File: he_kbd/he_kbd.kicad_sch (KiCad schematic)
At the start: 270 parts, among them J1 AudioJack4, J2 Conn_01x08_Pin, J3 AudioJack4, J4 Conn_01x08_Pin

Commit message: updated backside / right hand board swithc footprints to have no holes
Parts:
- HE_36, HE_37, HE_38, HE_39, HE_40, HE_41, HE_42, HE_43, HE_44, HE_45, HE_46, HE_47, HE_48, HE_49, HE_50, HE_51, HE_52, HE_53, HE_54, HE_55, HE_56, HE_57, HE_58, HE_59, HE_60, HE_61, HE_62, HE_63, HE_64, HE_65, HE_66, HE_67, HE_68, HE_69, HE_70: footprint he_kbd_footprint:Analogue_sensor_and_switch_profile -> he_kbd_footprint:Analogue_sensor_and_switch_profile_NO_HOLES
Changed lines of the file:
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@@
 			)
 		)
-		(property "Footprint" "he_kbd_footprint:Analogue_sensor_and_switch_profile"
+		(property "Footprint" "he_kbd_footprint:Analogue_sensor_and_switch_profile_NO_HOLES"
 			(at 472.186 107.696 0)
 			(effects
@@
 			)
 		)
-		(property "Footprint" "he_kbd_footprint:Analogue_sensor_and_switch_profile"
+		(property "Footprint" "he_kbd_footprint:Analogue_sensor_and_switch_profile_NO_HOLES"
 			(at 472.186 126.746 0)
 			(effects
@@
 			)
 		)
-		(property "Footprint" "he_kbd_footprint:Analogue_sensor_and_switch_profile"
+		(property "Footprint" "he_kbd_footprint:Analogue_sensor_and_switch_profile_NO_HOLES"
 			(at 557.276 120.396 0)
 			(effects
@@
 			)
 		)
-		(property "Footprint" "he_kbd_footprint:Analogue_sensor_and_switch_profile"
+		(property "Footprint" "he_kbd_footprint:Analogue_sensor_and_switch_profile_NO_HOLES"
 			(at 557.276 107.696 0)
 			(effects
@@
 			)
 		)
-		(property "Footprint" "he_kbd_footprint:Analogue_sensor_and_switch_profile"
+		(property "Footprint" "he_kbd_footprint:Analogue_sensor_and_switch_profile_NO_HOLES"
 			(at 435.864 86.614 0)
 			(effects
@@
 			)
 		)
-		(property "Footprint" "he_kbd_footprint:Analogue_sensor_and_switch_profile"
+		(property "Footprint" "he_kbd_footprint:Analogue_sensor_and_switch_profile_NO_HOLES"
 			(at 520.954 118.364 0)
 			(effects
@@
 			)
 		)
-		(property "Footprint" "he_kbd_footprint:Analogue_sensor_and_switch_profile"
+		(property "Footprint" "he_kbd_footprint:Analogue_sensor_and_switch_profile_NO_HOLES"
 			(at 520.954 131.064 0)
 			(effects
@@
 			)
 		)
-		(property "Footprint" "he_kbd_footprint:Analogue_sensor_and_switch_profile"
+		(property "Footprint" "he_kbd_footprint:Analogue_sensor_and_switch_profile_NO_HOLES"
 			(at 435.864 112.014 0)
 			(effects
@@
 			)
 		)
-		(property "Footprint" "he_kbd_footprint:Analogue_sensor_and_switch_profile"
+		(property "Footprint" "he_kbd_footprint:Analogue_sensor_and_switch_profile_NO_HOLES"
 			(at 520.954 112.014 0)
 			(effects
@@
 			)
 		)
-		(property "Footprint" "he_kbd_footprint:Analogue_sensor_and_switch_profile"
+		(property "Footprint" "he_kbd_footprint:Analogue_sensor_and_switch_profile_NO_HOLES"
 			(at 520.954 105.664 0)
 			(effects
@@
 			)
 		)
-		(property "Footprint" "he_kbd_footprint:Analogue_sensor_and_switch_profile"
+		(property "Footprint" "he_kbd_footprint:Analogue_sensor_and_switch_profile_NO_HOLES"
 			(at 557.276 114.046 0)
 			(effects
@@
 			)
 		)
-		(property "Footprint" "he_kbd_footprint:Analogue_sensor_and_switch_profile"
+		(property "Footprint" "he_kbd_footprint:Analogue_sensor_and_switch_profile_NO_HOLES"
 			(at 634.746 107.696 0)
 			(effects
@@
 			)
 		)
-		(property "Footprint" "he_kbd_footprint:Analogue_sensor_and_switch_profile"
+		(property "Footprint" "he_kbd_footprint:Analogue_sensor_and_switch_profile_NO_HOLES"
 			(at 472.186 133.096 0)
 			(effects
@@
 			)
 		)
-		(property "Footprint" "he_kbd_footprint:Analogue_sensor_and_switch_profile"
+		(property "Footprint" "he_kbd_footprint:Analogue_sensor_and_switch_profile_NO_HOLES"
 			(at 435.864 92.964 0)
 			(effects
@@
 			)
 		)
-		(property "Footprint" "he_kbd_footprint:Analogue_sensor_and_switch_profile"
+		(property "Footprint" "he_kbd_footprint:Analogue_sensor_and_switch_profile_NO_HOLES"
 			(at 557.276 139.446 0)
 			(effects
@@
 			)
 		)
-		(property "Footprint" "he_kbd_footprint:Analogue_sensor_and_switch_profile"
+		(property "Footprint" "he_kbd_footprint:Analogue_sensor_and_switch_profile_NO_HOLES"
 			(at 634.746 101.346 0)
 			(effects
@@
 			)
 		)
-		(property "Footprint" "he_kbd_footprint:Analogue_sensor_and_switch_profile"
+		(property "Footprint" "he_kbd_footprint:Analogue_sensor_and_switch_profile_NO_HOLES"
 			(at 557.276 94.996 0)
 			(effects
@@
 			)
 		)
-		(property "Footprint" "he_kbd_footprint:Analogue_sensor_and_switch_profile"
+		(property "Footprint" "he_kbd_footprint:Analogue_sensor_and_switch_profile_NO_HOLES"
 			(at 520.954 124.714 0)
 			(effects
@@
 			)
 		)
-		(property "Footprint" "he_kbd_footprint:Analogue_sensor_and_switch_profile"
+		(property "Footprint" "he_kbd_footprint:Analogue_sensor_and_switch_profile_NO_HOLES"
 			(at 435.864 118.364 0)
 			(effects
@@
 			)
 		)
-		(property "Footprint" "he_kbd_footprint:Analogue_sensor_and_switch_profile"
+		(property "Footprint" "he_kbd_footprint:Analogue_sensor_and_switch_profile_NO_HOLES"
 			(at 520.954 99.314 0)
 			(effects
@@
 			)
 		)
-		(property "Footprint" "he_kbd_footprint:Analogue_sensor_and_switch_profile"
+		(property "Footprint" "he_kbd_footprint:Analogue_sensor_and_switch_profile_NO_HOLES"
 			(at 472.186 139.446 0)
 			(effects
@@
 			)
 		)
-		(property "Footprint" "he_kbd_footprint:Analogue_sensor_and_switch_profile"
+		(property "Footprint" "he_kbd_footprint:Analogue_sensor_and_switch_profile_NO_HOLES"
 			(at 634.746 94.996 0)
 			(effects
@@
 			)
 		)
-		(property "Footprint" "he_kbd_footprint:Analogue_sensor_and_switch_profile"
+		(property "Footprint" "he_kbd_footprint:Analogue_sensor_and_switch_profile_NO_HOLES"
 			(at 435.864 124.714 0)
 			(effects
@@
 			)
 		)
-		(property "Footprint" "he_kbd_footprint:Analogue_sensor_and_switch_profile"
+		(property "Footprint" "he_kbd_footprint:Analogue_sensor_and_switch_profile_NO_HOLES"
 			(at 557.276 101.346 0)
 			(effects
@@
 			)
 		)
-		(property "Footprint" "he_kbd_footprint:Analogue_sensor_and_switch_profile"
+		(property "Footprint" "he_kbd_footprint:Analogue_sensor_and_switch_profile_NO_HOLES"
 			(at 472.186 101.346 0)
 			(effects
@@
 			)
 		)
-		(property "Footprint" "he_kbd_footprint:Analogue_sensor_and_switch_profile"
+		(property "Footprint" "he_kbd_footprint:Analogue_sensor_and_switch_profile_NO_HOLES"
 			(at 472.186 114.046 0)
 			(effects
@@
 			)
 		)
-		(property "Footprint" "he_kbd_footprint:Analogue_sensor_and_switch_profile"
+		(property "Footprint" "he_kbd_footprint:Analogue_sensor_and_switch_profile_NO_HOLES"
 			(at 435.864 99.314 0)
 			(effects
@@
 			)
 		)
-		(property "Footprint" "he_kbd_footprint:Analogue_sensor_and_switch_profile"
+		(property "Footprint" "he_kbd_footprint:Analogue_sensor_and_switch_profile_NO_HOLES"
 			(at 435.864 105.664 0)
 			(effects
@@
 			)
 		)
-		(property "Footprint" "he_kbd_footprint:Analogue_sensor_and_switch_profile"
+		(property "Footprint" "he_kbd_footprint:Analogue_sensor_and_switch_profile_NO_HOLES"
 			(at 557.276 126.746 0)
 			(effects
@@
 			)
 		)
-		(property "Footprint" "he_kbd_footprint:Analogue_sensor_and_switch_profile"
+		(property "Footprint" "he_kbd_footprint:Analogue_sensor_and_switch_profile_NO_HOLES"
 			(at 472.186 94.996 0)
 			(effects
@@
 			)
 		)
-		(property "Footprint" "he_kbd_footprint:Analogue_sensor_and_switch_profile"
+		(property "Footprint" "he_kbd_footprint:Analogue_sensor_and_switch_profile_NO_HOLES"
 			(at 472.186 120.396 0)
 			(effects
@@
 			)
 		)
-		(property "Footprint" "he_kbd_footprint:Analogue_sensor_and_switch_profile"
+		(property "Footprint" "he_kbd_footprint:Analogue_sensor_and_switch_profile_NO_HOLES"
 			(at 557.276 133.096 0)
 			(effects
@@
 			)
 		)
-		(property "Footprint" "he_kbd_footprint:Analogue_sensor_and_switch_profile"
+		(property "Footprint" "he_kbd_footprint:Analogue_sensor_and_switch_profile_NO_HOLES"
 			(at 520.954 92.964 0)
 			(effects
@@
 			)
 		)
-		(property "Footprint" "he_kbd_footprint:Analogue_sensor_and_switch_profile"
+		(property "Footprint" "he_kbd_footprint:Analogue_sensor_and_switch_profile_NO_HOLES"
 			(at 435.864 131.064 0)
 			(effects
@@
 			)
 		)
-		(property "Footprint" "he_kbd_footprint:Analogue_sensor_and_switch_profile"
+		(property "Footprint" "he_kbd_footprint:Analogue_sensor_and_switch_profile_NO_HOLES"
 			(at 520.954 86.614 0)
 			(effects

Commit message: updated schematic with labels for all the neopixel data connections
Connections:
- net NP_DAT11: now reaches D12.2 (DOUT), D13.4 (DIN)
- net NP_DAT11: now also D51.4 (DIN), D55.2 (DOUT)
- net NP_DAT10: now reaches D11.2 (DOUT), D12.4 (DIN)
- net NP_DAT10: now also D55.4 (DIN), D59.2 (DOUT)
- net NP_DAT15: now reaches D16.2 (DOUT), D17.4 (DIN)
- net NP_DAT15: now also D36.2 (DOUT), D38.4 (DIN)
- net NP_DAT14: now reaches D15.2 (DOUT), D16.4 (DIN)
- net NP_DAT14: now also D36.4 (DIN), D41.2 (DOUT)
- net NP_DAT7: now reaches D8.2 (DOUT), D9.4 (DIN)
- net NP_DAT7: now also D67.4 (DIN), D68.2 (DOUT)
- net NP_DAT6: now reaches D7.2 (DOUT), D8.4 (DIN)
- net NP_DAT6: now also D64.2 (DOUT), D68.4 (DIN)
- net NP_DAT4: now reaches D56.2 (DOUT), D60.4 (DIN)
- net NP_DAT4: now also D5.2 (DOUT), D6.4 (DIN)
- net NP_DAT3: now reaches D52.2 (DOUT), D56.4 (DIN)
- net NP_DAT3: now also D4.2 (DOUT), D5.4 (DIN)
- net NP_DAT5: now reaches D60.2 (DOUT), D64.4 (DIN)
- net NP_DAT5: now also D6.2 (DOUT), D7.4 (DIN)
- net NP_DAT26: now reaches D58.4 (DIN), D62.2 (DOUT)
- net NP_DAT26: now also D27.2 (DOUT), D28.4 (DIN)
- net NP_DAT1: now reaches D42.2 (DOUT), D47.4 (DIN)
- net NP_DAT1: now also D2.2 (DOUT), D3.4 (DIN)
- net NP_DAT0: now reaches D37.2 (DOUT), D42.4 (DIN)
- net NP_DAT0: now also D1.2 (DOUT), D2.4 (DIN)
- net NP_DAT13: now reaches D41.4 (DIN), D46.2 (DOUT)
- net NP_DAT13: now also D14.2 (DOUT), D15.4 (DIN)
- net NP_DAT12: now reaches D46.4 (DIN), D51.2 (DOUT)
- net NP_DAT12: now also D13.2 (DOUT), D14.4 (DIN)
- net NP_DAT21: now reaches D61.2 (DOUT), D65.4 (DIN)
- net NP_DAT21: now also D22.2 (DOUT), D23.4 (DIN)
- net NP_DAT20: now reaches D57.2 (DOUT), D61.4 (DIN)
- net NP_DAT20: now also D21.2 (DOUT), D22.4 (DIN)
- net NP_DAT18: now reaches D48.2 (DOUT), D53.4 (DIN)
- net NP_DAT18: now also D19.2 (DOUT), D20.4 (DIN)
- net NP_DAT17: now reaches D43.2 (DOUT), D48.4 (DIN)
- net NP_DAT17: now also D18.2 (DOUT), D19.4 (DIN)
- net NP_DAT2: now reaches D47.2 (DOUT), D52.4 (DIN)
- net NP_DAT2: now also D3.2 (DOUT), D4.4 (DIN)
- net NP_DAT33: now reaches D45.2 (DOUT), D50.4 (DIN)
- net NP_DAT33: now also D34.2 (DOUT), D35.4 (DIN)
- net NP_DAT32: now reaches D40.2 (DOUT), D45.4 (DIN)
- net NP_DAT32: now also D33.2 (DOUT), D34.4 (DIN)
- net NP_DAT29: now reaches D44.4 (DIN), D49.2 (DOUT)
- net NP_DAT29: now also D30.2 (DOUT), D31.4 (DIN)
- net NP_DAT16: now reaches D17.2 (DOUT), D18.4 (DIN)
- net NP_DAT16: now also D38.2 (DOUT), D43.4 (DIN)
- net NP_DAT31: now reaches D39.2 (DOUT), D40.4 (DIN)
- net NP_DAT31: now also D32.2 (DOUT), D33.4 (DIN)
- net NP_DAT30: now reaches D39.4 (DIN), D44.2 (DOUT)
- net NP_DAT30: now also D31.2 (DOUT), D32.4 (DIN)
- net NP_DAT23: now reaches D24.2 (DOUT), D25.4 (DIN)
- net NP_DAT23: now also D69.2 (DOUT), D70.4 (DIN)
- net NP_DAT8: now reaches D63.4 (DIN), D67.2 (DOUT)
- net NP_DAT8: now also D10.4 (DIN), D9.2 (DOUT)
- net NP_DAT22: now reaches D65.2 (DOUT), D69.4 (DIN)
- net NP_DAT22: now also D23.2 (DOUT), D24.4 (DIN)
- net NP_DAT9: now reaches D59.4 (DIN), D63.2 (DOUT)
- net NP_DAT9: now also D10.2 (DOUT), D11.4 (DIN)
- net NP_DAT19: now reaches D53.2 (DOUT), D57.4 (DIN)
- net NP_DAT19: now also D20.2 (DOUT), D21.4 (DIN)

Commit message: so far so good
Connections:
- net NP_DAT24: now also D66.4 (DIN), D70.2 (DOUT)
- net NP_DAT25: now also D62.4 (DIN), D66.2 (DOUT)
- net NP_DAT27: now also D54.4 (DIN), D58.2 (DOUT)
- net NP_DAT28: now also D49.4 (DIN), D54.2 (DOUT)
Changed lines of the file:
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@@
 	)
 	(label "NP_DAT25"
-		(at 524.51 271.7316 90)
+		(at 524.51 271.78 90)
 		(effects
 			(font
@@
 	)
 	(label "NP_DAT27"
-		(at 494.03 271.7316 90)
+		(at 494.03 271.78 90)
 		(effects
 			(font
@@
 	)
 	(label "NP_DAT24"
-		(at 539.75 271.7316 90)
+		(at 539.75 271.78 90)
 		(effects
 			(font
@@
 	)
 	(label "NP_DAT28"
-		(at 478.79 271.8222 90)
+		(at 478.79 271.78 90)
 		(effects
 			(font

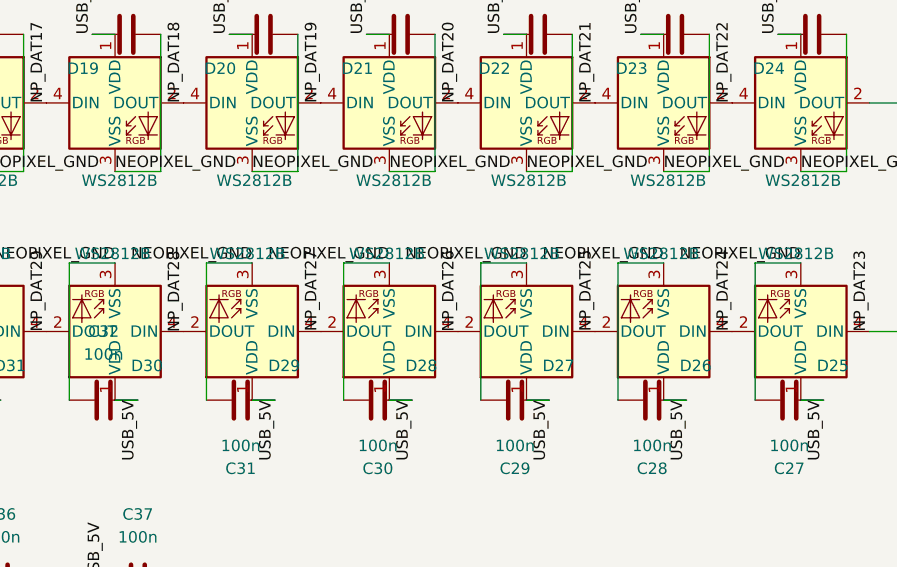
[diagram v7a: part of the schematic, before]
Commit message: wired up the easy mtp
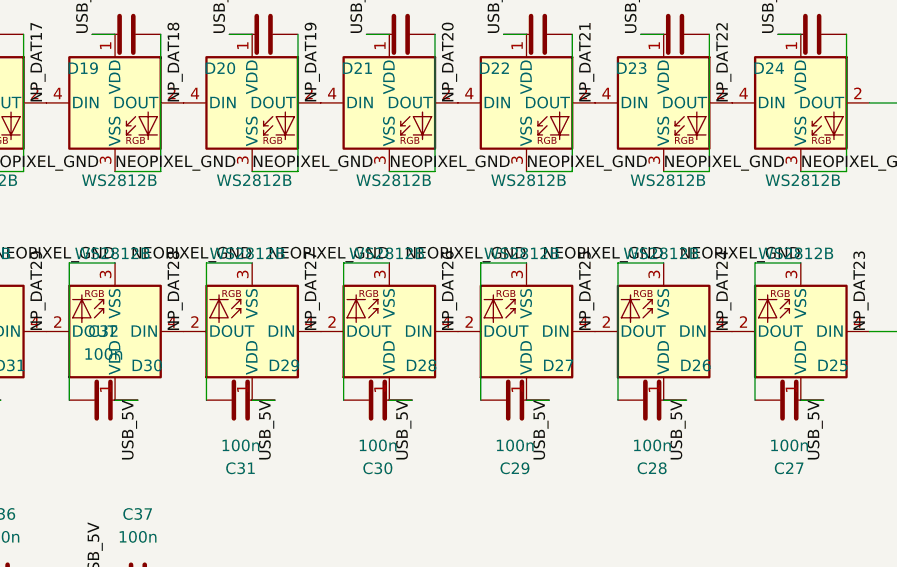
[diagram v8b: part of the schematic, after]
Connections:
- net NP_DAT24: now also D25.2 (DOUT), D26.4 (DIN)
- net NP_DAT25: now also D26.2 (DOUT), D27.4 (DIN)
- net NP_DAT27: now also D28.2 (DOUT), D29.4 (DIN)
- net NP_DAT28: now also D29.2 (DOUT), D30.4 (DIN)
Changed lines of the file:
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@@
 	)
 	(label "NP_DAT28"
-		(at 119.38 287.0622 90)
+		(at 119.38 287.02 90)
 		(effects
 			(font
@@
 	)
 	(label "NP_DAT24"
-		(at 180.34 286.9716 90)
+		(at 180.34 287.02 90)
 		(effects
 			(font
@@
 	)
 	(label "NP_DAT25"
-		(at 165.1 286.9716 90)
+		(at 165.1 287.02 90)
 		(effects
 			(font
@@
 	)
 	(label "NP_DAT27"
-		(at 134.62 286.9716 90)
+		(at 134.62 287.02 90)
 		(effects
 			(font
